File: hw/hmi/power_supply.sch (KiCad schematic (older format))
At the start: 20 parts, among them U7 TS1117BCW33, U8 MCP1603T-330

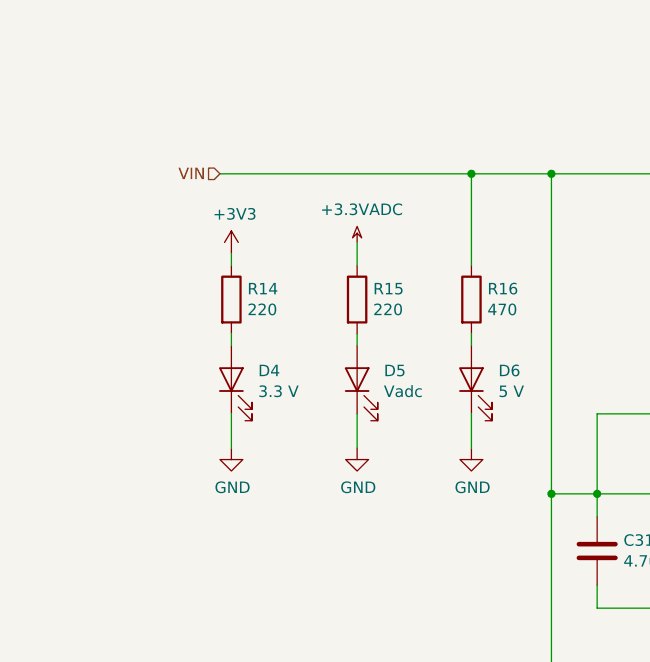
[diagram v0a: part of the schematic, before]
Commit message: Added HMI and SDU boards
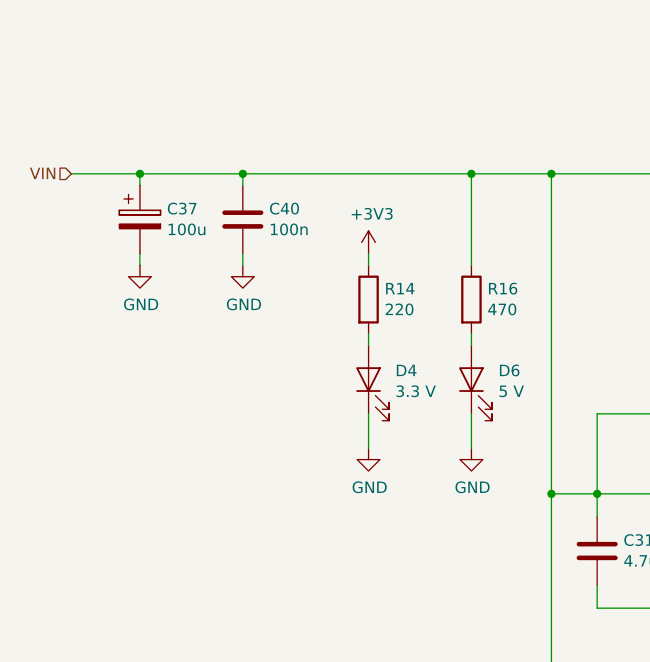
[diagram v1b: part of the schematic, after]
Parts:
- removed D5: Vadc, LED_SMD:LED_1206_3216Metric, symbol Device:LED
- removed R15: 220, Resistor_SMD:R_0805_2012Metric, symbol Device:R
- added C37: 100u, Capacitor_SMD:CP_Elec_6.3x7.7, symbol Device:CP
- added C40: 100n, Capacitor_SMD:C_0805_2012Metric, symbol Device:C
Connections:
- net GND: now also C37.2, C40.2
- net VIN: now also C37.1, C40.1
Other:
- moved on the sheet: D4, R14
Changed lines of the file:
@@
 Comment4 ""
 $EndDescr
-Text HLabel 3350 3000 0    50   Input ~ 0
+Text HLabel 2700 3000 0    50   Input ~ 0
 VIN
 $Comp
@@
 L Device:LED D4
 U 1 1 5C37AFE9
-P 3400 3900
-F 0 "D4" V 3438 3783 50  0000 R CNN
-F 1 "3.3 V" V 3347 3783 50  0000 R CNN
-F 2 "LED_SMD:LED_1206_3216Metric" H 3400 3900 50  0001 C CNN
-F 3 "~" H 3400 3900 50  0001 C CNN
-	1    3400 3900
+P 4000 3900
+F 0 "D4" V 4038 3783 50  0000 R CNN
+F 1 "3.3 V" V 3947 3783 50  0000 R CNN
+F 2 "LED_SMD:LED_1206_3216Metric" H 4000 3900 50  0001 C CNN
+F 3 "~" H 4000 3900 50  0001 C CNN
+	1    4000 3900
 	0    -1   -1   0
 $EndComp
@@
 L Device:R R14
 U 1 1 5C37B05F
-P 3400 3550
-F 0 "R14" H 3470 3596 50  0000 L CNN
-F 1 "220" H 3470 3505 50  0000 L CNN
-F 2 "Resistor_SMD:R_0805_2012Metric" V 3330 3550 50  0001 C CNN
-F 3 "~" H 3400 3550 50  0001 C CNN
-	1    3400 3550
-	1    0    0    -1
-$EndComp
-Wire Wire Line
-	3400 3700 3400 3750
+P 4000 3550
+F 0 "R14" H 4070 3596 50  0000 L CNN
+F 1 "220" H 4070 3505 50  0000 L CNN
+F 2 "Resistor_SMD:R_0805_2012Metric" V 3930 3550 50  0001 C CNN
+F 3 "~" H 4000 3550 50  0001 C CNN
+	1    4000 3550
+	1    0    0    -1
+$EndComp
+Wire Wire Line
+	4000 3700 4000 3750
 $Comp
 L power:GND #PWR0160
 U 1 1 5C37B20A
-P 3400 4200
-F 0 "#PWR0160" H 3400 3950 50  0001 C CNN
-F 1 "GND" H 3405 4027 50  0000 C CNN
-F 2 "" H 3400 4200 50  0001 C CNN
-F 3 "" H 3400 4200 50  0001 C CNN
-	1    3400 4200
-	1    0    0    -1
-$EndComp
-Wire Wire Line
-	3400 4200 3400 4050
+P 4000 4200
+F 0 "#PWR0160" H 4000 3950 50  0001 C CNN
+F 1 "GND" H 4005 4027 50  0000 C CNN
+F 2 "" H 4000 4200 50  0001 C CNN
+F 3 "" H 4000 4200 50  0001 C CNN
+	1    4000 4200
+	1    0    0    -1
+$EndComp
+Wire Wire Line
+	4000 4200 4000 4050
 $Comp
 L power:+3V3 #PWR0161
 U 1 1 5C37B3FC
-P 3400 3350
-F 0 "#PWR0161" H 3400 3200 50  0001 C CNN
-F 1 "+3V3" H 3415 3523 50  0000 C CNN
-F 2 "" H 3400 3350 50  0001 C CNN
-F 3 "" H 3400 3350 50  0001 C CNN
-	1    3400 3350
-	1    0    0    -1
-$EndComp
-Wire Wire Line
-	3400 3350 3400 3400
-$Comp
-L Device:LED D5
-U 1 1 5C37B5E1
-P 3950 3900
-F 0 "D5" V 3988 3783 50  0000 R CNN
-F 1 "Vadc" V 3897 3783 50  0000 R CNN
-F 2 "LED_SMD:LED_1206_3216Metric" H 3950 3900 50  0001 C CNN
-F 3 "~" H 3950 3900 50  0001 C CNN
-	1    3950 3900
-	0    -1   -1   0
-$EndComp
-$Comp
-L Device:R R15
-U 1 1 5C37B5E7
-P 3950 3550
-F 0 "R15" H 4020 3596 50  0000 L CNN
-F 1 "220" H 4020 3505 50  0000 L CNN
-F 2 "Resistor_SMD:R_0805_2012Metric" V 3880 3550 50  0001 C CNN
-F 3 "~" H 3950 3550 50  0001 C CNN
-	1    3950 3550
-	1    0    0    -1
-$EndComp
-Wire Wire Line
-	3950 3700 3950 3750
-$Comp
-L power:GND #PWR0162
-U 1 1 5C37B5EE
-P 3950 4200
-F 0 "#PWR0162" H 3950 3950 50  0001 C CNN
-F 1 "GND" H 3955 4027 50  0000 C CNN
-F 2 "" H 3950 4200 50  0001 C CNN
-F 3 "" H 3950 4200 50  0001 C CNN
-	1    3950 4200
-	1    0    0    -1
-$EndComp
-Wire Wire Line
-	3950 4200 3950 4050
-Wire Wire Line
-	3950 3300 3950 3400
+P 4000 3350
+F 0 "#PWR0161" H 4000 3200 50  0001 C CNN
+F 1 "+3V3" H 4015 3523 50  0000 C CNN
+F 2 "" H 4000 3350 50  0001 C CNN
+F 3 "" H 4000 3350 50  0001 C CNN
+	1    4000 3350
+	1    0    0    -1
+$EndComp
+Wire Wire Line
+	4000 3350 4000 3400
 $Comp
 L Device:LED D6
@@
 $EndComp
 Wire Wire Line
-	3350 3000 4450 3000
-$Comp
-L power:+3.3VADC #PWR0165
-U 1 1 5C4232C5
-P 3950 3300
-F 0 "#PWR0165" H 4100 3250 50  0001 C CNN
-F 1 "+3.3VADC" H 3970 3443 50  0000 C CNN
-F 2 "" H 3950 3300 50  0001 C CNN
-F 3 "" H 3950 3300 50  0001 C CNN
-	1    3950 3300
-	1    0    0    -1
-$EndComp
+	2700 3000 3000 3000
 Wire Wire Line
 	4450 3400 4450 3000
@@
 Wire Wire Line
 	9200 1050 9200 950
+$Comp
+L Device:CP C37
+U 1 1 5C207C40
+P 3000 3200
+F 0 "C37" H 3118 3246 50  0000 L CNN
+F 1 "100u" H 3118 3155 50  0000 L CNN
+F 2 "Capacitor_SMD:CP_Elec_6.3x7.7" H 3038 3050 50  0001 C CNN
+F 3 "~" H 3000 3200 50  0001 C CNN
+	1    3000 3200
+	1    0    0    -1
+$EndComp
+Wire Wire Line
+	3000 3050 3000 3000
+Connection ~ 3000 3000
+Wire Wire Line
+	3000 3000 3450 3000
+$Comp
+L power:GND #PWR0130
+U 1 1 5C2090CE
+P 3000 3400
+F 0 "#PWR0130" H 3000 3150 50  0001 C CNN
+F 1 "GND" H 3005 3227 50  0000 C CNN
+F 2 "" H 3000 3400 50  0001 C CNN
+F 3 "" H 3000 3400 50  0001 C CNN
+	1    3000 3400
+	1    0    0    -1
+$EndComp
+Wire Wire Line
+	3000 3400 3000 3350
+$Comp
+L Device:C C40
+U 1 1 5C20C385
+P 3450 3200
+F 0 "C40" H 3565 3246 50  0000 L CNN
+F 1 "100n" H 3565 3155 50  0000 L CNN
+F 2 "Capacitor_SMD:C_0805_2012Metric" H 3488 3050 50  0001 C CNN
+F 3 "~" H 3450 3200 50  0001 C CNN
+	1    3450 3200
+	1    0    0    -1
+$EndComp
+$Comp
+L power:GND #PWR0162
+U 1 1 5C20C466
+P 3450 3400
+F 0 "#PWR0162" H 3450 3150 50  0001 C CNN
+F 1 "GND" H 3455 3227 50  0000 C CNN
+F 2 "" H 3450 3400 50  0001 C CNN
+F 3 "" H 3450 3400 50  0001 C CNN
+	1    3450 3400
+	1    0    0    -1
+$EndComp
+Wire Wire Line
+	3450 3400 3450 3350
+Wire Wire Line
+	3450 3050 3450 3000
+Connection ~ 3450 3000
+Wire Wire Line
+	3450 3000 4450 3000
 $EndSCHEMATC

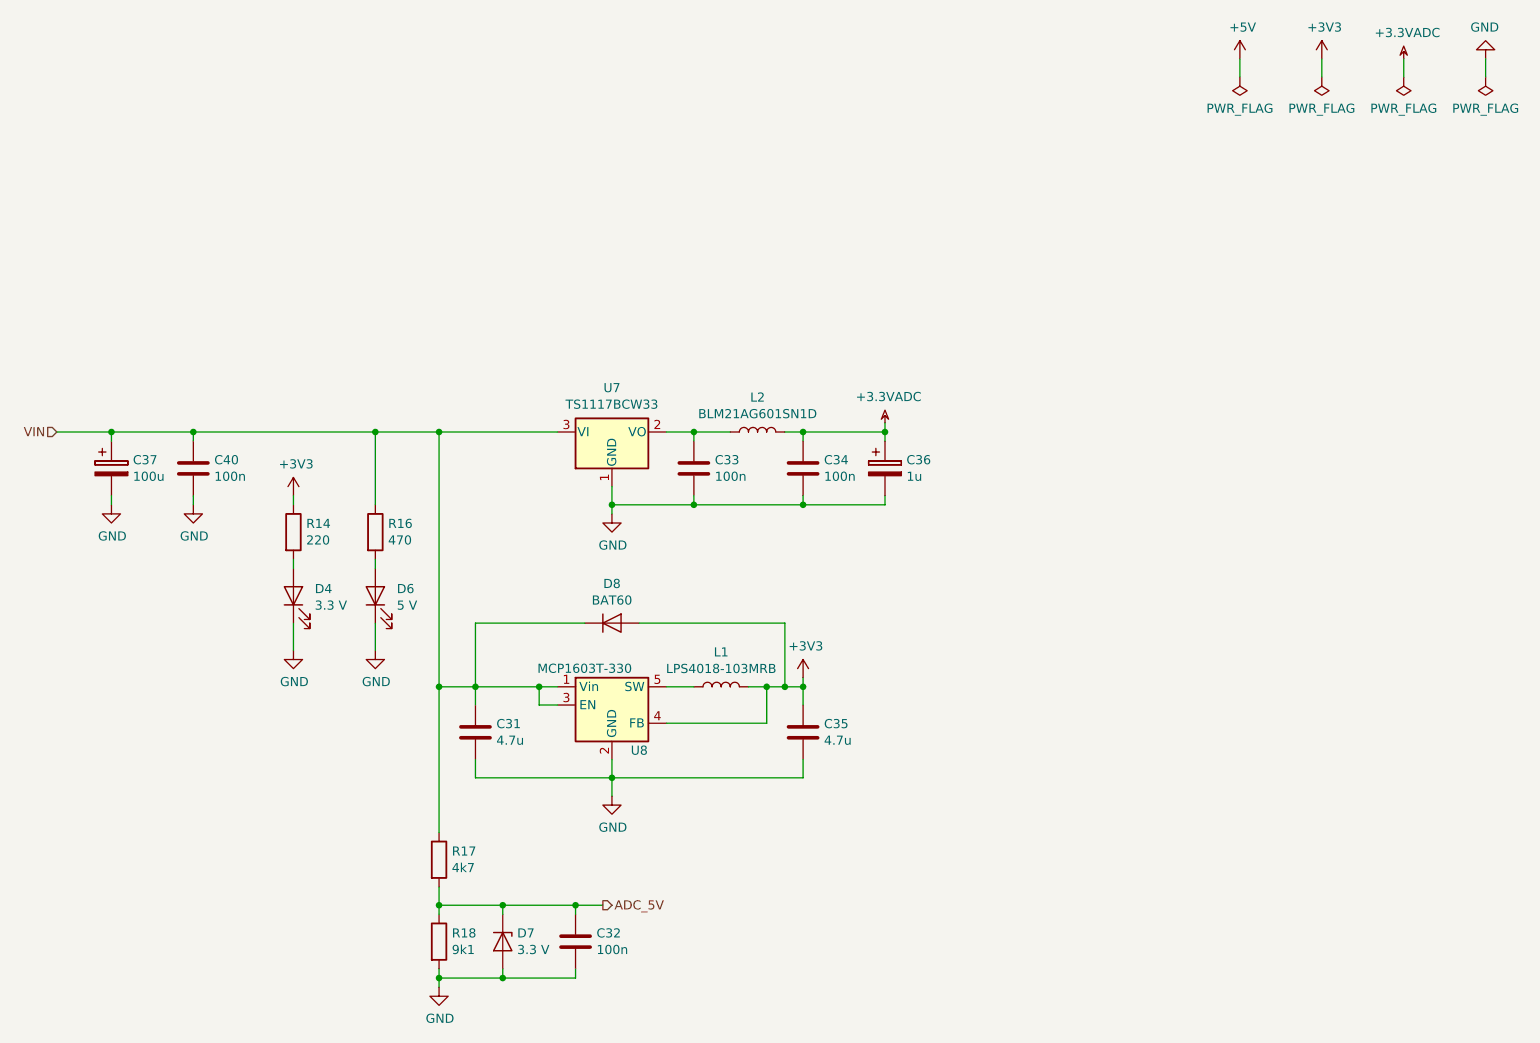
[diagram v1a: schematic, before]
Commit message: Updated power supply in HMI
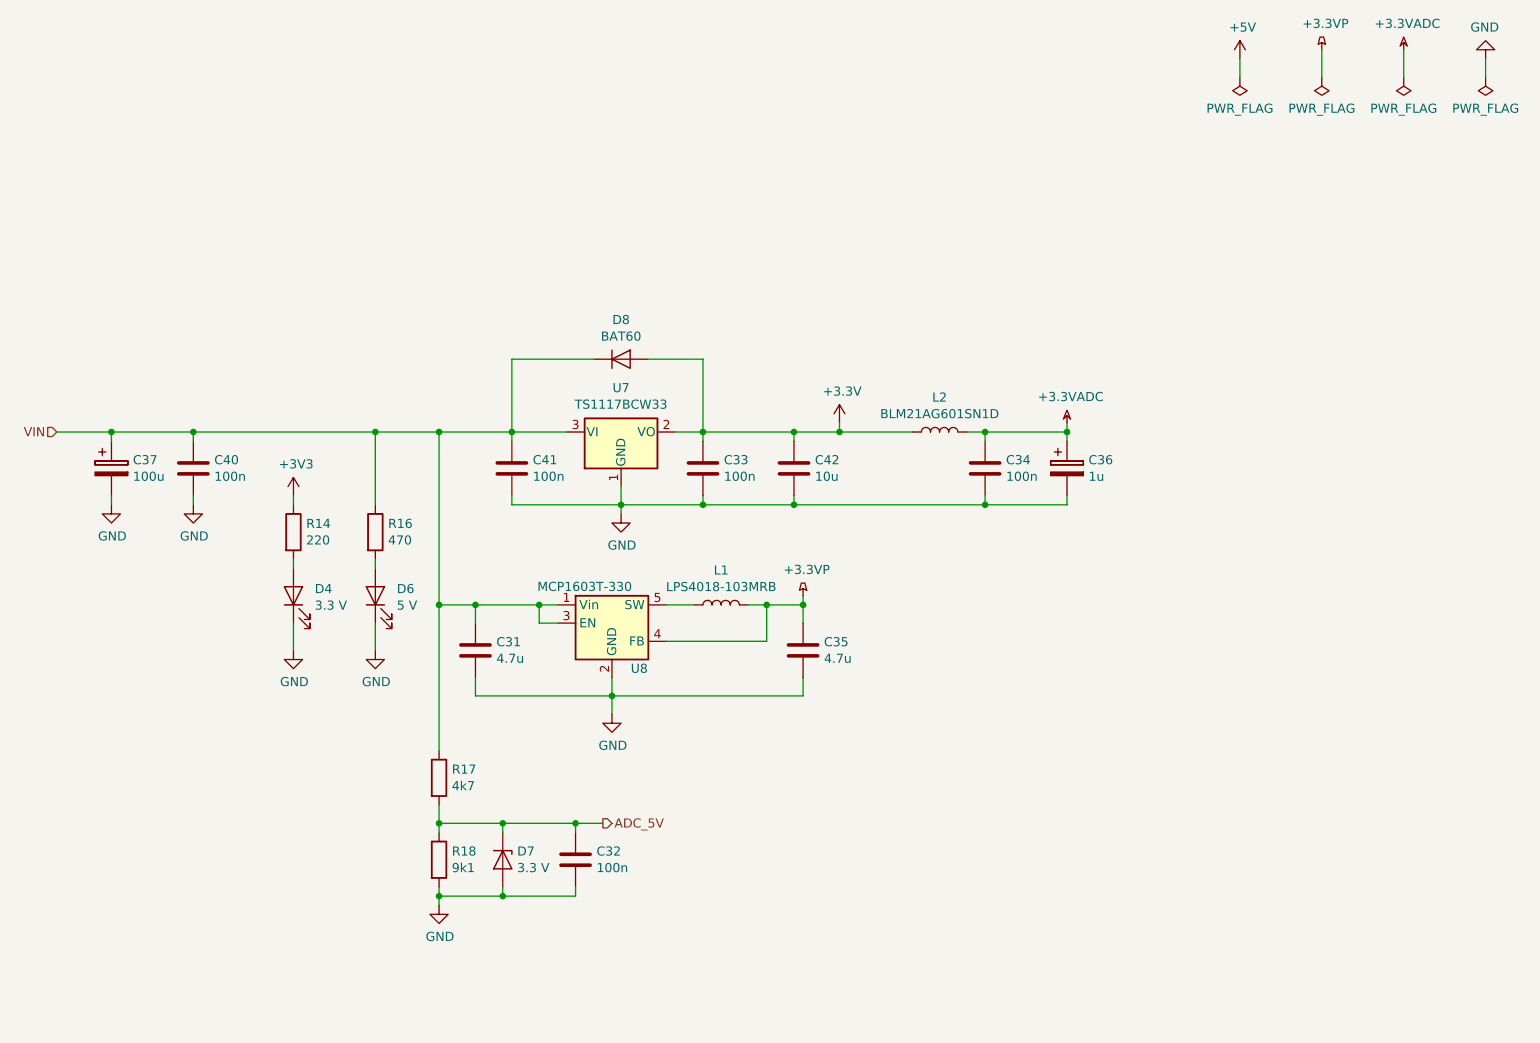
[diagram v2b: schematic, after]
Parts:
- added C41: 100n, Capacitor_SMD:C_0805_2012Metric, symbol Device:C
- added C42: 10u, Capacitor_SMD:C_0805_2012Metric, symbol Device:C
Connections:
- net +3V3: now also C33.1, L2.1, U7.2 (VO), C42.1; no longer C35.1, L1.2, U8.4 (FB)
- net GND: now also C41.2, C42.2
- net VIN: now also C41.1
- new net +3.3VP: C35.1, L1.2, U8.4 (FB)
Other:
- moved on the sheet: C31, C32, C33, C34, C35, C36, D7, D8, L1, L2, R17, R18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
